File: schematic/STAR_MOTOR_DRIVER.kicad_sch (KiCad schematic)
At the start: 46 parts, among them J1 6120XX21621_61200821621, J10 B6B-XH-A, J11 B6B-XH-A, J12 B6B-XH-A, J2 6120XX21621_61200621621, J3 B6B-XH-A, J4 6120XX21621_61200821621, J5 6120XX21621_61200821621, J6 6120XX21621_61200821621, J7 1017491, U1 DRV8243SQDGQRQ1 (S-Variant), U2 DRV8243SQDGQRQ1 (S-Variant), U3 DRV8243SQDGQRQ1 (S-Variant), U4 DRV8243SQDGQRQ1 (S-Variant)

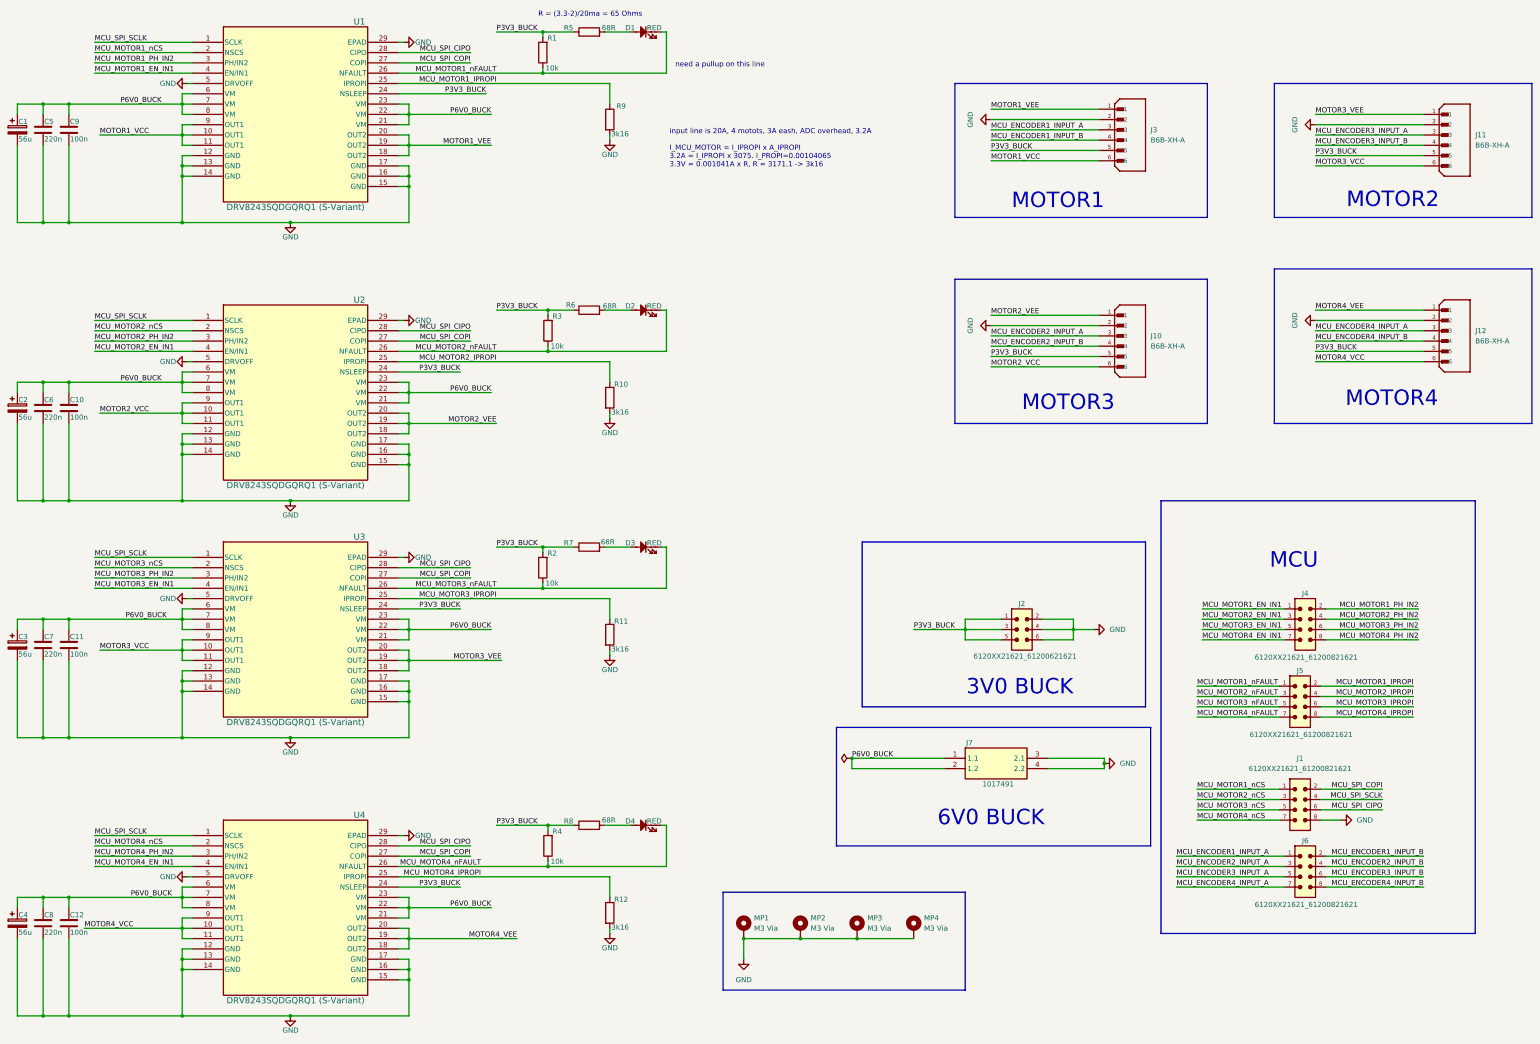
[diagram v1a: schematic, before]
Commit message: add motor driver SPI documentation and PMOD footprint
- Add motor driver SPI configuration to hardware pinout documentation
  - Add purple color legend for Motor Driver SPI
  - Update 7 pins (85, 86, 69, 70, 29, 25, 18) with RSPI2 SPI functions
  - SCLK (PD1), COPI (PD0), CIPO (PA1)
  - nCS0 (P17), nCS1 (P23), nCS2 (P32), nCS3 (PA0)
- Add Motor Driver Dual-Interface Architecture section
  - Explains PWM for real-time control vs SPI for configuration
- Remove PMOD JD section (repurposed for motor driver SPI)
- Update STAR_MOTOR_DRIVER.kicad_sch motor numbering (MOTOR1-4 to MOTOR0-3)
- Add 5-534998-6 PMOD connector footprint to symbols-and-footprints
  - TE Connectivity 2x6 header connector
  - Includes KiCad symbol, footprint, and 3D models
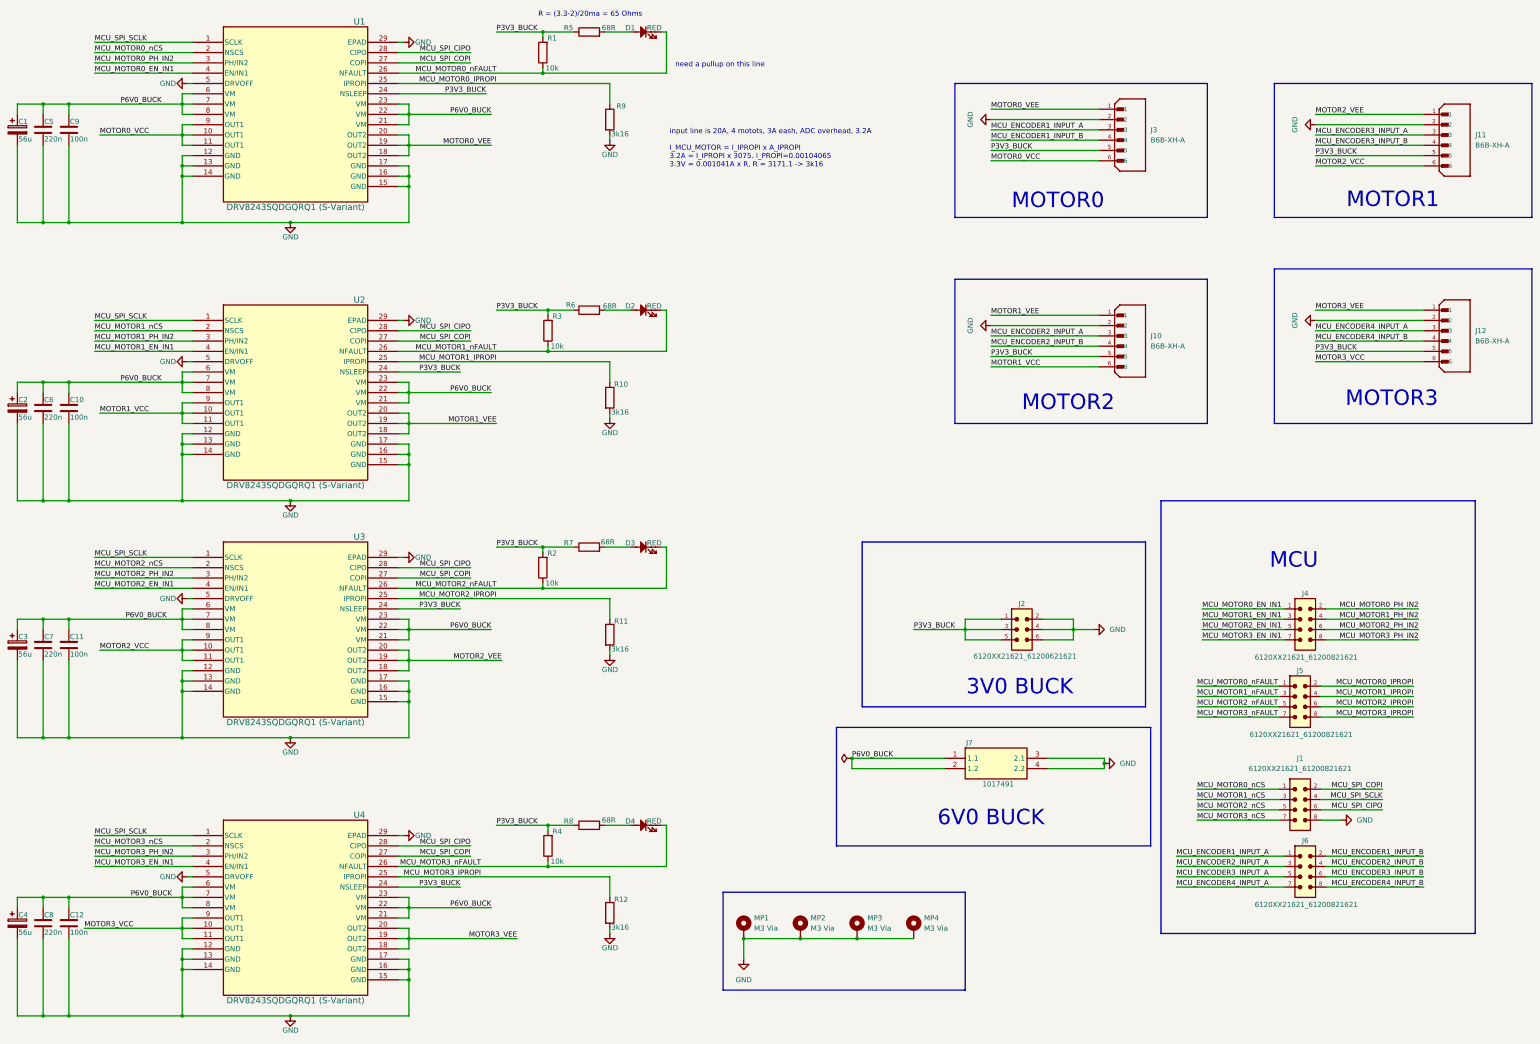
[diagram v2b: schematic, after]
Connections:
- net MCU_MOTOR4_EN_IN1 is gone; now on net MCU_MOTOR3_EN_IN1: J4.7, U4.4 (EN/IN1)
- net MCU_MOTOR4_IPROPI is gone; now on net MCU_MOTOR3_IPROPI: J5.8, R12.1, U4.25 (IPROPI)
- net MCU_MOTOR4_PH_IN2 is gone; now on net MCU_MOTOR3_PH_IN2: J4.8, U4.3 (PH/IN2)
- net MCU_MOTOR4_nCS is gone; now on net MCU_MOTOR3_nCS: J1.7, U4.2 (NSCS)
- net MCU_MOTOR4_nFAULT is gone; now on net MCU_MOTOR3_nFAULT: D4.1, J5.7, R4.1, U4.26 (NFAULT)
- net MOTOR4_VCC is gone; now on net MOTOR3_VCC: J12.6, U4.10 (OUT1), U4.11 (OUT1), U4.9 (OUT1)
- net MOTOR4_VEE is gone; now on net MOTOR3_VEE: J12.1, U4.18 (OUT2), U4.19 (OUT2), U4.20 (OUT2)
- net MCU_MOTOR1_EN_IN1: now also J4.3, U2.4 (EN/IN1); no longer J4.1, U1.4 (EN/IN1)
- net MCU_MOTOR1_IPROPI: now also J5.4, R10.1, U2.25 (IPROPI); no longer J5.2, R9.1, U1.25 (IPROPI)
- net MCU_MOTOR1_PH_IN2: now also J4.4, U2.3 (PH/IN2); no longer J4.2, U1.3 (PH/IN2)
- net MCU_MOTOR1_nCS: now also J1.3, U2.2 (NSCS); no longer J1.1, U1.2 (NSCS)
- net MCU_MOTOR1_nFAULT: now also D2.1, J5.3, R3.1, U2.26 (NFAULT); no longer D1.1, J5.1, R1.1, U1.26 (NFAULT)
- net MCU_MOTOR2_EN_IN1: now also J4.5, U3.4 (EN/IN1); no longer J4.3, U2.4 (EN/IN1)
- net MCU_MOTOR2_IPROPI: now also J5.6, R11.1, U3.25 (IPROPI); no longer J5.4, R10.1, U2.25 (IPROPI)
- net MCU_MOTOR2_PH_IN2: now also J4.6, U3.3 (PH/IN2); no longer J4.4, U2.3 (PH/IN2)
- net MCU_MOTOR2_nCS: now also J1.5, U3.2 (NSCS); no longer J1.3, U2.2 (NSCS)
- net MCU_MOTOR2_nFAULT: now also D3.1, J5.5, R2.1, U3.26 (NFAULT); no longer D2.1, J5.3, R3.1, U2.26 (NFAULT)
- net MCU_MOTOR3_EN_IN1: no longer J4.5, U3.4 (EN/IN1)
- net MCU_MOTOR3_IPROPI: no longer J5.6, R11.1, U3.25 (IPROPI)
- net MCU_MOTOR3_PH_IN2: no longer J4.6, U3.3 (PH/IN2)
- net MCU_MOTOR3_nCS: no longer J1.5, U3.2 (NSCS)
- net MCU_MOTOR3_nFAULT: no longer D3.1, J5.5, R2.1, U3.26 (NFAULT)
- net MOTOR1_VCC: now also J10.6, U2.10 (OUT1), U2.11 (OUT1), U2.9 (OUT1); no longer J3.6, U1.10 (OUT1), U1.11 (OUT1), U1.9 (OUT1)
- net MOTOR1_VEE: now also J10.1, U2.18 (OUT2), U2.19 (OUT2), U2.20 (OUT2); no longer J3.1, U1.18 (OUT2), U1.19 (OUT2), U1.20 (OUT2)
- net MOTOR2_VCC: now also J11.6, U3.10 (OUT1), U3.11 (OUT1), U3.9 (OUT1); no longer J10.6, U2.10 (OUT1), U2.11 (OUT1), U2.9 (OUT1)
- net MOTOR2_VEE: now also J11.1, U3.18 (OUT2), U3.19 (OUT2), U3.20 (OUT2); no longer J10.1, U2.18 (OUT2), U2.19 (OUT2), U2.20 (OUT2)
- net MOTOR3_VCC: no longer J11.6, U3.10 (OUT1), U3.11 (OUT1), U3.9 (OUT1)
- net MOTOR3_VEE: no longer J11.1, U3.18 (OUT2), U3.19 (OUT2), U3.20 (OUT2)
- new net MCU_MOTOR0_EN_IN1: J4.1, U1.4 (EN/IN1)
- new net MCU_MOTOR0_IPROPI: J5.2, R9.1, U1.25 (IPROPI)
- new net MCU_MOTOR0_PH_IN2: J4.2, U1.3 (PH/IN2)
- new net MCU_MOTOR0_nCS: J1.1, U1.2 (NSCS)
- new net MCU_MOTOR0_nFAULT: D1.1, J5.1, R1.1, U1.26 (NFAULT)
- new net MOTOR0_VCC: J3.6, U1.10 (OUT1), U1.11 (OUT1), U1.9 (OUT1)
- new net MOTOR0_VEE: J3.1, U1.18 (OUT2), U1.19 (OUT2), U1.20 (OUT2)
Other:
- note added: "MOTOR0"
- note removed: "MOTOR4"
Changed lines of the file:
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@@
 		)
 	)
-	(text "MOTOR2"
+	(text "MOTOR1"
 		(exclude_from_sim no)
 		(at 361.95 69.342 0)
@@
 		)
 	)
-	(text "MOTOR4\n"
+	(text "MOTOR3\n"
 		(exclude_from_sim no)
 		(at 361.696 118.364 0)
@@
 		)
 	)
-	(text "MOTOR1"
+	(text "MOTOR0"
 		(exclude_from_sim no)
 		(at 279.4 69.596 0)
@@
 		)
 	)
-	(text "MOTOR3\n"
+	(text "MOTOR2\n"
 		(exclude_from_sim no)
 		(at 281.94 119.38 0)
@@
 		)
 	)
-	(label "MOTOR4_VEE"
+	(label "MOTOR3_VEE"
 		(at 146.05 251.46 180)
 		(effects
@@
 		)
 	)
-	(label "MCU_MOTOR4_nCS"
+	(label "MCU_MOTOR3_nCS"
 		(at 313.69 222.25 0)
 		(effects
@@
 		)
 	)
-	(label "MCU_MOTOR3_nFAULT"
+	(label "MCU_MOTOR2_nFAULT"
 		(at 140.97 165.1 180)
 		(effects
@@
 		)
 	)
-	(label "MCU_MOTOR3_IPROPI"
+	(label "MCU_MOTOR2_IPROPI"
 		(at 140.97 167.64 180)
 		(effects
@@
 		)
 	)
-	(label "MOTOR1_VCC"
+	(label "MOTOR0_VCC"
 		(at 262.89 59.69 0)
 		(effects
@@
 		)
 	)
-	(label "MOTOR2_VEE"
+	(label "MOTOR1_VEE"
 		(at 140.97 124.46 180)
 		(effects
@@
 		)
 	)
-	(label "MCU_MOTOR3_PH_IN2"
+	(label "MCU_MOTOR2_PH_IN2"
 		(at 368.3 175.26 180)
 		(effects
@@
 		)
 	)
-	(label "MCU_MOTOR3_EN_IN1"
+	(label "MCU_MOTOR2_EN_IN1"
 		(at 314.96 175.26 0)
 		(effects
@@
 		)
 	)
-	(label "MCU_MOTOR2_IPROPI"
+	(label "MCU_MOTOR1_IPROPI"
 		(at 367.03 191.77 180)
 		(effects
@@
 		)
 	)
-	(label "MOTOR1_VCC"
+	(label "MOTOR0_VCC"
 		(at 43.18 53.34 0)
 		(effects
@@
 		)
 	)
-	(label "MCU_MOTOR1_nCS"
+	(label "MCU_MOTOR0_nCS"
 		(at 313.69 214.63 0)
 		(effects
@@
 		)
 	)
-	(label "MCU_MOTOR2_nCS"
+	(label "MCU_MOTOR1_nCS"
 		(at 41.91 101.6 0)
 		(effects
@@
 		)
 	)
-	(label "MCU_MOTOR2_EN_IN1"
+	(label "MCU_MOTOR1_EN_IN1"
 		(at 314.96 172.72 0)
 		(effects
@@
 		)
 	)
-	(label "MCU_MOTOR3_nFAULT"
+	(label "MCU_MOTOR2_nFAULT"
 		(at 313.69 194.31 0)
 		(effects
@@
 		)
 	)
-	(label "MCU_MOTOR2_nCS"
+	(label "MCU_MOTOR1_nCS"
 		(at 313.69 217.17 0)
 		(effects
@@
 		)
 	)
-	(label "MCU_MOTOR1_EN_IN1"
+	(label "MCU_MOTOR0_EN_IN1"
 		(at 314.96 170.18 0)
 		(effects
@@
 		)
 	)
-	(label "MOTOR4_VCC"
+	(label "MOTOR3_VCC"
 		(at 342.9 109.22 0)
 		(effects
@@
 		)
 	)
-	(label "MOTOR1_VEE"
+	(label "MOTOR0_VEE"
 		(at 262.89 46.99 0)
 		(effects
@@
 		)
 	)
-	(label "MOTOR4_VCC"
+	(label "MOTOR3_VCC"
 		(at 39.37 248.92 0)
 		(effects
@@
 		)
 	)
-	(label "MOTOR2_VCC"
+	(label "MOTOR1_VCC"
 		(at 43.18 121.92 0)
 		(effects
@@
 		)
 	)
-	(label "MCU_MOTOR2_nFAULT"
+	(label "MCU_MOTOR1_nFAULT"
 		(at 140.97 106.68 180)
 		(effects
@@
 		)
 	)
-	(label "MOTOR3_VEE"
+	(label "MOTOR2_VEE"
 		(at 142.24 182.88 180)
 		(effects
@@
 		)
 	)
-	(label "MCU_MOTOR3_nCS"
+	(label "MCU_MOTOR2_nCS"
 		(at 41.91 160.02 0)
 		(effects
@@
 		)
 	)
-	(label "MOTOR2_VCC"
+	(label "MOTOR1_VCC"
 		(at 262.89 110.49 0)
 		(effects
@@
 		)
 	)
-	(label "MCU_MOTOR2_IPROPI"
+	(label "MCU_MOTOR1_IPROPI"
 		(at 140.97 109.22 180)
 		(effects
@@
 		)
 	)
-	(label "MCU_MOTOR4_IPROPI"
+	(label "MCU_MOTOR3_IPROPI"
 		(at 137.16 236.22 180)
 		(effects
@@
 		)
 	)
-	(label "MCU_MOTOR3_IPROPI"
+	(label "MCU_MOTOR2_IPROPI"
 		(at 367.03 194.31 180)
 		(effects
@@
 		)
 	)
-	(label "MCU_MOTOR2_nFAULT"
+	(label "MCU_MOTOR1_nFAULT"
 		(at 313.69 191.77 0)
 		(effects
@@
 		)
 	)
-	(label "MCU_MOTOR1_PH_IN2"
+	(label "MCU_MOTOR0_PH_IN2"
 		(at 368.3 170.18 180)
 		(effects
@@
 		)
 	)
-	(label "MCU_MOTOR4_EN_IN1"
+	(label "MCU_MOTOR3_EN_IN1"
 		(at 314.96 177.8 0)
 		(effects
@@
 		)
 	)
-	(label "MCU_MOTOR4_nFAULT"
+	(label "MCU_MOTOR3_nFAULT"
 		(at 313.69 196.85 0)
 		(effects
@@
 		)
 	)
-	(label "MCU_MOTOR4_EN_IN1"
+	(label "MCU_MOTOR3_EN_IN1"
 		(at 41.91 233.68 0)
 		(effects
@@
 		)
 	)
-	(label "MCU_MOTOR1_PH_IN2"
+	(label "MCU_MOTOR0_PH_IN2"
 		(at 41.91 35.56 0)
 		(effects
@@
 		)
 	)
-	(label "MOTOR3_VCC"
+	(label "MOTOR2_VCC"
 		(at 342.9 60.96 0)
 		(effects
@@
 		)
 	)
-	(label "MCU_MOTOR1_nFAULT"
+	(label "MCU_MOTOR0_nFAULT"
 		(at 313.69 189.23 0)
 		(effects
@@
 		)
 	)
-	(label "MOTOR1_VEE"
+	(label "MOTOR0_VEE"
 		(at 139.7 55.88 180)
 		(effects
@@
 		)
 	)
-	(label "MCU_MOTOR2_PH_IN2"
+	(label "MCU_MOTOR1_PH_IN2"
 		(at 368.3 172.72 180)
 		(effects
@@
 		)
 	)
-	(label "MCU_MOTOR3_nCS"
+	(label "MCU_MOTOR2_nCS"
 		(at 313.69 219.71 0)
 		(effects
@@
 		)
 	)
-	(label "MOTOR3_VCC"
+	(label "MOTOR2_VCC"
 		(at 43.18 180.34 0)
 		(effects
@@
 		)
 	)
-	(label "MCU_MOTOR1_IPROPI"
+	(label "MCU_MOTOR0_IPROPI"
 		(at 140.97 40.64 180)
 		(effects
@@
 		)
 	)
-	(label "MCU_MOTOR1_nCS"
+	(label "MCU_MOTOR0_nCS"
 		(at 41.91 33.02 0)
 		(effects
@@
 		)
 	)
-	(label "MCU_MOTOR4_PH_IN2"
+	(label "MCU_MOTOR3_PH_IN2"
 		(at 368.3 177.8 180)
 		(effects
@@
 		)
 	)
-	(label "MCU_MOTOR1_IPROPI"
+	(label "MCU_MOTOR0_IPROPI"
 		(at 367.03 189.23 180)
 		(effects
@@
 		)
 	)
-	(label "MCU_MOTOR4_PH_IN2"
+	(label "MCU_MOTOR3_PH_IN2"
 		(at 41.91 231.14 0)
 		(effects
@@
 		)
 	)
-	(label "MCU_MOTOR4_nCS"
+	(label "MCU_MOTOR3_nCS"
 		(at 41.91 228.6 0)
 		(effects
@@
 		)
 	)
-	(label "MOTOR2_VEE"
+	(label "MOTOR1_VEE"
 		(at 262.89 97.79 0)
 		(effects
@@
 		)
 	)
-	(label "MCU_MOTOR3_PH_IN2"
+	(label "MCU_MOTOR2_PH_IN2"
 		(at 41.91 162.56 0)
 		(effects
@@
 		)
 	)
-	(label "MCU_MOTOR1_EN_IN1"
+	(label "MCU_MOTOR0_EN_IN1"
 		(at 41.91 38.1 0)
 		(effects
@@
 		)
 	)
-	(label "MCU_MOTOR1_nFAULT"
+	(label "MCU_MOTOR0_nFAULT"
 		(at 140.97 38.1 180)
 		(effects
@@
 		)
 	)
-	(label "MCU_MOTOR4_IPROPI"
+	(label "MCU_MOTOR3_IPROPI"
 		(at 367.03 196.85 180)
 		(effects
@@
 		)
 	)
-	(label "MCU_MOTOR4_nFAULT"
+	(label "MCU_MOTOR3_nFAULT"
 		(at 137.16 233.68 180)
 		(effects
@@
 		)
 	)
-	(label "MCU_MOTOR2_PH_IN2"
+	(label "MCU_MOTOR1_PH_IN2"
 		(at 41.91 104.14 0)
 		(effects
@@
 		)
 	)
-	(label "MOTOR4_VEE"
+	(label "MOTOR3_VEE"
 		(at 342.9 96.52 0)
 		(effects
@@
 		)
 	)
-	(label "MCU_MOTOR3_EN_IN1"
+	(label "MCU_MOTOR2_EN_IN1"
 		(at 41.91 165.1 0)
 		(effects
@@
 		)
 	)
-	(label "MOTOR3_VEE"
+	(label "MOTOR2_VEE"
 		(at 342.9 48.26 0)
 		(effects
@@
 		)
 	)
-	(label "MCU_MOTOR2_EN_IN1"
+	(label "MCU_MOTOR1_EN_IN1"
 		(at 41.91 106.68 0)
 		(effects

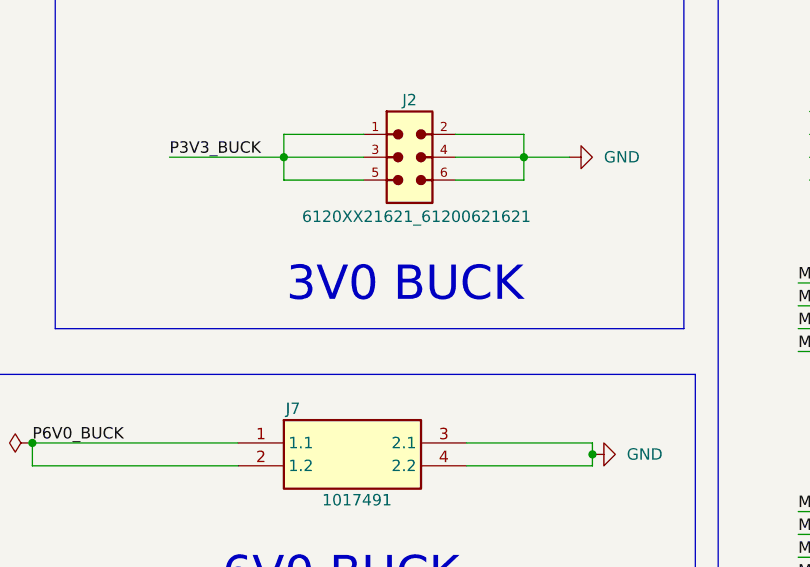
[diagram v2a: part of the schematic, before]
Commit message: Rename STAR_BUS to STAR_BMS (Battery Management System)
File Renames:
- STAR_BUS.kicad_sch → STAR_BMS.kicad_sch
- STAR_BUS.kicad_pro → STAR_BMS.kicad_pro
- STAR_BUS.kicad_pcb → STAR_BMS.kicad_pcb
- STAR_BUS.kicad_prl → STAR_BMS.kicad_prl (not tracked)
- STAR_BUS-backups/ → STAR_BMS-backups/

Internal Reference Updates:
- Updated all "STAR_BUS" references to "STAR_BMS" in project files
- Updated cross-references in STAR_MOTOR_DRIVER and STAR_POWER_BOARD

Corrects naming to properly reflect Battery Management System (BMS)
instead of BUS.
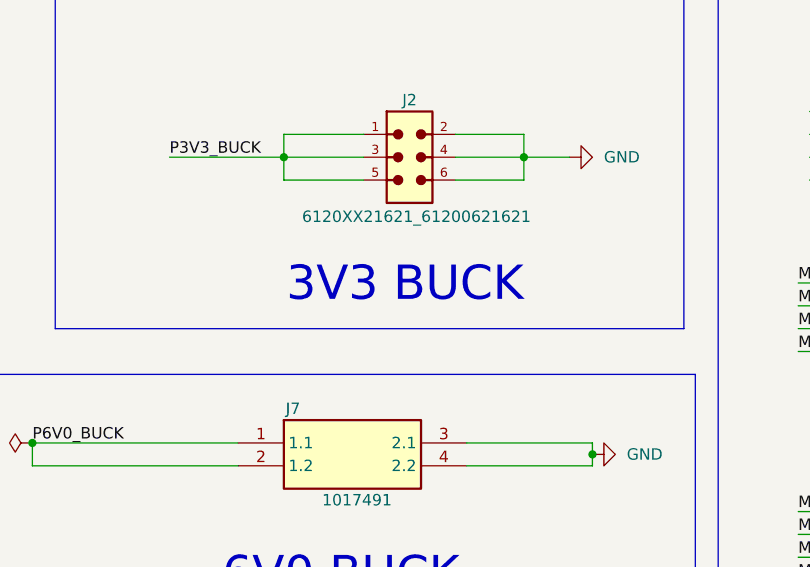
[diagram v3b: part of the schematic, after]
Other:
- note added: "3V3 BUCK"
- note removed: "3V0 BUCK"
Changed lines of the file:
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@@
 		)
 	)
-	(text "3V0 BUCK"
+	(text "3V3 BUCK"
 		(exclude_from_sim no)
 		(at 270.002 189.484 0)
